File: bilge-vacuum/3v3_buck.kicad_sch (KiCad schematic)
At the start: 24 parts, among them Q1 PSMN014-80YL, Q2 PSMN014-80YL, U4 LTC3851

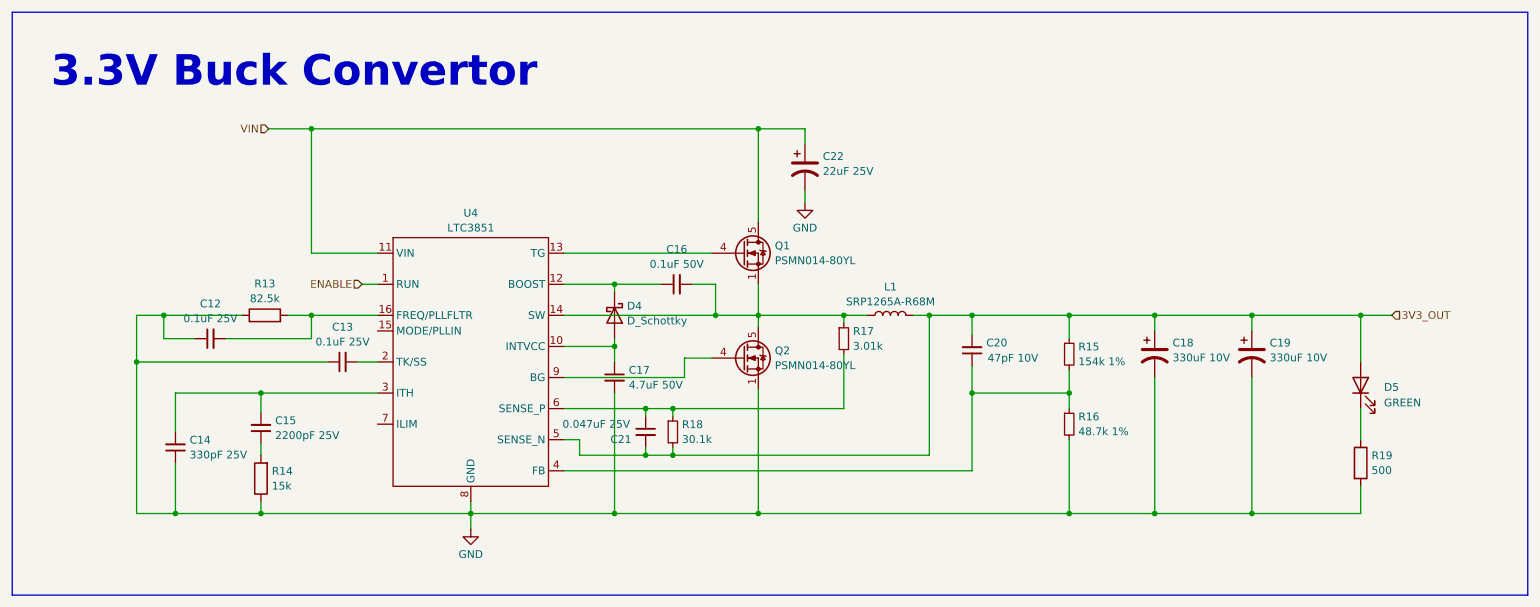
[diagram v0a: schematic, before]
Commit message: Assign the bulk of parts, some passives still need custom footprints.
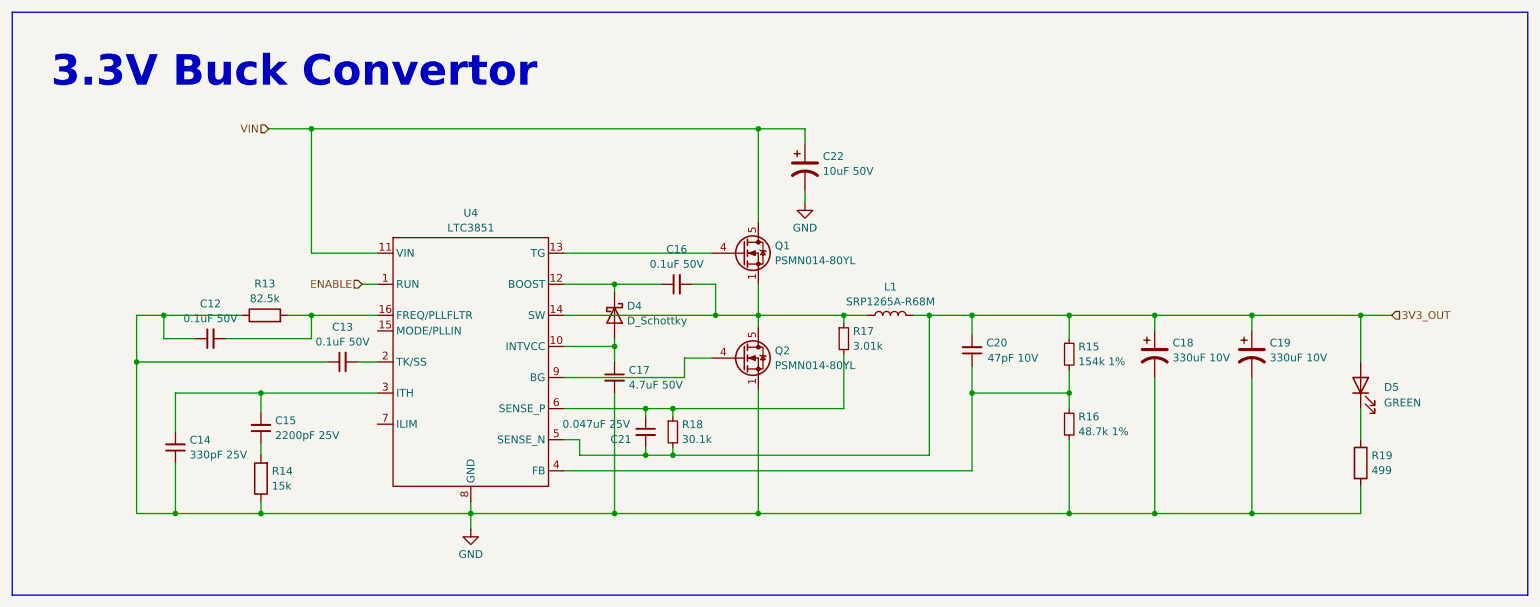
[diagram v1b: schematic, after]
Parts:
- C12, C13: value 0.1uF 25V -> 0.1uF 50V; footprint (none) -> Capacitor_SMD:C_0805_2012Metric
- C14, C15, C16, C17, C20, C21: footprint (none) -> Capacitor_SMD:C_0805_2012Metric
- C22: value 22uF 25V -> 10uF 50V; footprint (none) -> Capacitor_SMD:C_1206_3216Metric
- D4: footprint (none) -> Custom Parts:SMA
- D5: footprint (none) -> LED_SMD:LED_0805_2012Metric
- R13, R14, R15, R16, R17, R18: footprint (none) -> Resistor_SMD:R_0805_2012Metric
- R19: value 500 -> 499; footprint (none) -> Resistor_SMD:R_0805_2012Metric
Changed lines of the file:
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@@
       (effects (font (size 1.27 1.27)) (justify right))
     )
-    (property "Footprint" "" (at 239.395 80.01 0)
+    (property "Footprint" "LED_SMD:LED_0805_2012Metric" (at 239.395 80.01 0)
       (effects (font (size 1.27 1.27)) hide)
     )
@@
       (effects (font (size 1.27 1.27)) (justify left))
     )
-    (property "Footprint" "" (at 117.475 78.74 0)
+    (property "Footprint" "Capacitor_SMD:C_0805_2012Metric" (at 117.475 78.74 0)
       (effects (font (size 1.27 1.27)) hide)
     )
@@
       (effects (font (size 1.27 1.27)) (justify left))
     )
-    (property "Footprint" "" (at 127 87.63 0)
+    (property "Footprint" "Resistor_SMD:R_0805_2012Metric" (at 127 87.63 0)
       (effects (font (size 1.27 1.27)) hide)
     )
@@
       (effects (font (size 1.27 1.27)) (justify right))
     )
-    (property "Footprint" "" (at 61.468 95.25 90)
+    (property "Footprint" "Resistor_SMD:R_0805_2012Metric" (at 61.468 95.25 90)
       (effects (font (size 1.27 1.27)) hide)
     )
@@
       (effects (font (size 1.27 1.27)) (justify left))
     )
-    (property "Footprint" "" (at 117.475 68.58 0)
+    (property "Footprint" "Custom Parts:SMA" (at 117.475 68.58 0)
       (effects (font (size 1.27 1.27)) hide)
     )
@@
       (effects (font (size 1.27 1.27)) (justify right))
     )
-    (property "Footprint" "" (at 175.895 74.295 0)
+    (property "Footprint" "Capacitor_SMD:C_0805_2012Metric" (at 175.895 74.295 0)
       (effects (font (size 1.27 1.27)) hide)
     )
@@
       (effects (font (size 1.27 1.27)))
     )
-    (property "Value" "0.1uF 25V" (at 51.4413 69.1078 90)
-      (effects (font (size 1.27 1.27)))
-    )
-    (property "Footprint" "" (at 51.435 72.39 0)
+    (property "Value" "0.1uF 50V" (at 51.4413 69.1078 90)
+      (effects (font (size 1.27 1.27)))
+    )
+    (property "Footprint" "Capacitor_SMD:C_0805_2012Metric" (at 51.435 72.39 0)
       (effects (font (size 1.27 1.27)) hide)
     )
@@
       (effects (font (size 1.27 1.27)) (justify right))
     )
-    (property "Footprint" "" (at 122.555 87.63 0)
+    (property "Footprint" "Capacitor_SMD:C_0805_2012Metric" (at 122.555 87.63 0)
       (effects (font (size 1.27 1.27)) hide)
     )
@@
       (effects (font (size 1.27 1.27)) (justify left))
     )
-    (property "Footprint" "" (at 154.94 72.39 0)
+    (property "Footprint" "Resistor_SMD:R_0805_2012Metric" (at 154.94 72.39 0)
       (effects (font (size 1.27 1.27)) hide)
     )
@@
       (effects (font (size 1.27 1.27)) (justify right))
     )
-    (property "Footprint" "" (at 59.69 86.995 0)
+    (property "Footprint" "Capacitor_SMD:C_0805_2012Metric" (at 59.69 86.995 0)
       (effects (font (size 1.27 1.27)) hide)
     )
@@
       (effects (font (size 1.27 1.27)))
     )
-    (property "Value" "0.1uF 25V" (at 73.0313 72.9178 90)
-      (effects (font (size 1.27 1.27)))
-    )
-    (property "Footprint" "" (at 73.025 76.2 0)
+    (property "Value" "0.1uF 50V" (at 73.0313 72.9178 90)
+      (effects (font (size 1.27 1.27)))
+    )
+    (property "Footprint" "Capacitor_SMD:C_0805_2012Metric" (at 73.025 76.2 0)
       (effects (font (size 1.27 1.27)) hide)
     )
@@
       (effects (font (size 1.27 1.27)) (justify left))
     )
-    (property "Footprint" "" (at 191.77 74.93 0)
+    (property "Footprint" "Resistor_SMD:R_0805_2012Metric" (at 191.77 74.93 0)
       (effects (font (size 1.27 1.27)) hide)
     )
@@
       (effects (font (size 1.27 1.27)))
     )
-    (property "Footprint" "" (at 60.325 70.358 90)
+    (property "Footprint" "Resistor_SMD:R_0805_2012Metric" (at 60.325 70.358 90)
       (effects (font (size 1.27 1.27)) hide)
     )
@@
       (effects (font (size 1.27 1.27)) (justify left))
     )
-    (property "Value" "22uF 25V" (at 151.511 45.0271 0)
-      (effects (font (size 1.27 1.27)) (justify left))
-    )
-    (property "Footprint" "" (at 148.59 44.45 0)
+    (property "Value" "10uF 50V" (at 151.511 45.0271 0)
+      (effects (font (size 1.27 1.27)) (justify left))
+    )
+    (property "Footprint" "Capacitor_SMD:C_1206_3216Metric" (at 148.59 44.45 0)
       (effects (font (size 1.27 1.27)) hide)
     )
@@
       (effects (font (size 1.27 1.27)))
     )
-    (property "Footprint" "" (at 127.635 63.5 0)
+    (property "Footprint" "Capacitor_SMD:C_0805_2012Metric" (at 127.635 63.5 0)
       (effects (font (size 1.27 1.27)) hide)
     )
@@
       (effects (font (size 1.27 1.27)) (justify right))
     )
-    (property "Footprint" "" (at 45.72 90.17 0)
+    (property "Footprint" "Capacitor_SMD:C_0805_2012Metric" (at 45.72 90.17 0)
       (effects (font (size 1.27 1.27)) hide)
     )
@@
       (effects (font (size 1.27 1.27)) (justify left))
     )
-    (property "Value" "500" (at 241.173 93.9221 0)
-      (effects (font (size 1.27 1.27)) (justify left))
-    )
-    (property "Footprint" "" (at 237.617 92.71 90)
+    (property "Value" "499" (at 241.173 93.9221 0)
+      (effects (font (size 1.27 1.27)) (justify left))
+    )
+    (property "Footprint" "Resistor_SMD:R_0805_2012Metric" (at 237.617 92.71 90)
       (effects (font (size 1.27 1.27)) hide)
     )
@@
       (effects (font (size 1.27 1.27)) (justify left))
     )
-    (property "Footprint" "" (at 191.77 86.36 0)
-      (effects (font (size 1.27 1.27)) hide)
-    )
+    (property "Footprint" "Resistor_SMD:R_0805_2012Metric" (at 191.77 86.36 0)
+      (effects (font (size 1.27 1.27)) hide)
+    )

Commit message: Vac progress
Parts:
- C18, C19: value 330uF 10V -> EEE-FK1A331AV; footprint (none) -> Custom Parts:Panasonic - F - Vibe
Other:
- moved on the sheet: C19
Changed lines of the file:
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@@
     (stroke (width 0) (type default))
   )
-  (wire (pts (xy 221.615 78.74) (xy 221.615 100.965))
+  (wire (pts (xy 221.615 90.17) (xy 221.615 100.965))
     (stroke (width 0) (type default))
   )
@@
     (stroke (width 0) (type default))
   )
-  (wire (pts (xy 221.615 68.58) (xy 221.615 71.12))
+  (wire (pts (xy 221.615 68.58) (xy 221.615 82.55))
     (stroke (width 0) (type default))
   )
@@
       (effects (font (size 1.27 1.27)) (justify left))
     )
-    (property "Value" "330uF 10V" (at 208.661 75.5071 0)
-      (effects (font (size 1.27 1.27)) (justify left))
-    )
-    (property "Footprint" "" (at 205.74 74.93 0)
+    (property "Value" "EEE-FK1A331AV" (at 208.661 75.5071 0)
+      (effects (font (size 1.27 1.27)) (justify left))
+    )
+    (property "Footprint" "Custom Parts:Panasonic - F - Vibe" (at 205.74 74.93 0)
       (effects (font (size 1.27 1.27)) hide)
     )
@@
     )
   )
-  (symbol (lib_id "Device:C_Polarized_US") (at 221.615 74.93 0) (unit 1)
-    (in_bom yes) (on_board yes) (dnp no) (fields_autoplaced)
-    (property "Reference" "C19" (at 224.536 73.0829 0)
-      (effects (font (size 1.27 1.27)) (justify left))
-    )
-    (property "Value" "330uF 10V" (at 224.536 75.5071 0)
-      (effects (font (size 1.27 1.27)) (justify left))
-    )
-    (property "Footprint" "" (at 221.615 74.93 0)
-      (effects (font (size 1.27 1.27)) hide)
-    )
-    (property "Datasheet" "~" (at 221.615 74.93 0)
-      (effects (font (size 1.27 1.27)) hide)
-    )
+  (symbol (lib_id "Device:C_Polarized_US") (at 221.615 86.36 0) (unit 1)
+    (in_bom yes) (on_board yes) (dnp no) (fields_autoplaced)
+    (property "Reference" "C19" (at 224.536 84.5129 0)
+      (effects (font (size 1.27 1.27)) (justify left))
+    )
+    (property "Value" "EEE-FK1A331AV" (at 224.536 86.9371 0)
+      (effects (font (size 1.27 1.27)) (justify left))
+    )
+    (property "Footprint" "Custom Parts:Panasonic - F - Vibe" (at 221.615 86.36 0)
+      (effects (font (size 1.27 1.27)) hide)
+    )
+    (property "Datasheet" "~" (at 221.615 86.36 0)
+      (effects (font (size 1.27 1.27)) hide)
+    )

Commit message: bilge vac 1v0
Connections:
- net BUCK_BG: now reaches Q2.4 (G), U4.9 (BG)
- net BUCK_TG: now reaches Q1.4 (G), U4.13 (TG)
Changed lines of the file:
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@@
     (effects (font (size 5 5) bold) (justify left bottom))
+  )
+  (label "BUCK_TG" (at 111.76 58.42 0) (fields_autoplaced)
+    (effects (font (size 1.27 1.27)) (justify left bottom))
+  )
+  (label "BUCK_BG" (at 111.76 78.74 0) (fields_autoplaced)
+    (effects (font (size 1.27 1.27)) (justify left bottom))
   )
   (hierarchical_label "3V3_OUT" (shape input) (at 244.475 68.58 0) (fields_autoplaced)

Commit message: Fixes
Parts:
- added C22 (x2): 10uF 50V, Capacitor_SMD:C_1206_3216Metric, symbol Device:C_Small
- C22: symbol Device:C_Polarized_US -> Device:C_Small
- D4: value D_Schottky -> B260AQ-13-F
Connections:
- net GND: now also C22.2, C22.2
- net VIN: now also C22.1, C22.1
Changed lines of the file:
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@@
   (junction (at 205.74 100.965) (diameter 0) (color 0 0 0 0)
   )
+  (junction (at 163.83 38.1) (diameter 0) (color 0 0 0 0)
+  )
   (junction (at 117.475 73.66) (diameter 0) (color 0 0 0 0)
   )
   (junction (at 59.69 81.28) (diameter 0) (color 0 0 0 0)
   )
+  (junction (at 148.59 50.8) (diameter 0) (color 0 0 0 0)
+  )
   (junction (at 175.895 81.28) (diameter 0) (color 0 0 0 0)
   )
+  (junction (at 148.59 38.1) (diameter 0) (color 0 0 0 0)
+  )
   (junction (at 122.555 83.82) (diameter 0) (color 0 0 0 0)
   )
@@
   (junction (at 140.97 100.965) (diameter 0) (color 0 0 0 0)
   )
+  (junction (at 163.83 50.8) (diameter 0) (color 0 0 0 0)
+  )
   (junction (at 191.77 81.28) (diameter 0) (color 0 0 0 0)
   )
@@
     (stroke (width 0) (type default))
   )
+  (wire (pts (xy 163.83 47.625) (xy 163.83 50.8))
+    (stroke (width 0) (type default))
+  )
   (wire (pts (xy 67.945 58.42) (xy 67.945 38.1))
     (stroke (width 0) (type default))
@@
     (stroke (width 0) (type default))
   )
-  (wire (pts (xy 148.59 40.64) (xy 148.59 38.1))
-    (stroke (width 0) (type default))
-  )
   (wire (pts (xy 140.97 38.1) (xy 140.97 53.34))
     (stroke (width 0) (type default))
@@
     (stroke (width 0) (type default))
   )
+  (wire (pts (xy 163.83 50.8) (xy 179.07 50.8))
+    (stroke (width 0) (type default))
+  )
   (wire (pts (xy 239.395 68.58) (xy 239.395 76.2))
     (stroke (width 0) (type default))
@@
     (stroke (width 0) (type default))
   )
+  (wire (pts (xy 148.59 50.8) (xy 148.59 52.705))
+    (stroke (width 0) (type default))
+  )
   (wire (pts (xy 39.37 76.2) (xy 39.37 68.58))
     (stroke (width 0) (type default))
@@
     (stroke (width 0) (type default))
   )
+  (wire (pts (xy 148.59 38.1) (xy 148.59 42.545))
+    (stroke (width 0) (type default))
+  )
   (wire (pts (xy 59.69 81.28) (xy 45.72 81.28))
     (stroke (width 0) (type default))
   )
+  (wire (pts (xy 148.59 50.8) (xy 163.83 50.8))
+    (stroke (width 0) (type default))
+  )
   (wire (pts (xy 78.74 58.42) (xy 67.945 58.42))
     (stroke (width 0) (type default))
@@
     (stroke (width 0) (type default))
   )
+  (wire (pts (xy 163.83 38.1) (xy 179.07 38.1))
+    (stroke (width 0) (type default))
+  )
+  (wire (pts (xy 148.59 38.1) (xy 163.83 38.1))
+    (stroke (width 0) (type default))
+  )
   (wire (pts (xy 59.69 100.965) (xy 59.69 99.06))
     (stroke (width 0) (type default))
@@
     (stroke (width 0) (type default))
   )
+  (wire (pts (xy 179.07 47.625) (xy 179.07 50.8))
+    (stroke (width 0) (type default))
+  )
   (wire (pts (xy 127 83.82) (xy 122.555 83.82))
     (stroke (width 0) (type default))
@@
     (stroke (width 0) (type default))
   )
+  (wire (pts (xy 179.07 38.1) (xy 179.07 42.545))
+    (stroke (width 0) (type default))
+  )
   (wire (pts (xy 205.74 68.58) (xy 221.615 68.58))
     (stroke (width 0) (type default))
@@
     (stroke (width 0) (type default))
   )
+  (wire (pts (xy 163.83 38.1) (xy 163.83 42.545))
+    (stroke (width 0) (type default))
+  )
   (wire (pts (xy 43.815 68.58) (xy 43.815 72.39))
     (stroke (width 0) (type default))
@@
     (stroke (width 0) (type default))
   )
-  (wire (pts (xy 148.59 48.26) (xy 148.59 50.165))
-    (stroke (width 0) (type default))
-  )
   (wire (pts (xy 221.615 68.58) (xy 239.395 68.58))
     (stroke (width 0) (type default))
@@
   )
   (wire (pts (xy 205.74 68.58) (xy 205.74 71.12))
+    (stroke (width 0) (type default))
+  )
+  (wire (pts (xy 148.59 47.625) (xy 148.59 50.8))
     (stroke (width 0) (type default))
   )
@@
       (effects (font (size 1.27 1.27)) (justify left))
     )
-    (property "Value" "D_Schottky" (at 119.507 69.4746 90)
+    (property "Value" "B260AQ-13-F" (at 119.507 69.4746 90)
       (effects (font (size 1.27 1.27)) (justify left))
     )
@@
     )
   )
-  (symbol (lib_id "power:GND") (at 148.59 50.165 0) (unit 1)
-    (in_bom yes) (on_board yes) (dnp no) (fields_autoplaced)
-    (property "Reference" "#PWR018" (at 148.59 56.515 0)
-      (effects (font (size 1.27 1.27)) hide)
-    )
-    (property "Value" "GND" (at 148.59 54.2981 0)
+  (symbol (lib_id "power:GND") (at 148.59 52.705 0) (unit 1)
+    (in_bom yes) (on_board yes) (dnp no) (fields_autoplaced)
+    (property "Reference" "#PWR018" (at 148.59 59.055 0)
+      (effects (font (size 1.27 1.27)) hide)
+    )
+    (property "Value" "GND" (at 148.59 56.8381 0)
       (effects (font (size 1.27 1.27)))
     )
-    (property "Footprint" "" (at 148.59 50.165 0)
-      (effects (font (size 1.27 1.27)) hide)
-    )
-    (property "Datasheet" "" (at 148.59 50.165 0)
+    (property "Footprint" "" (at 148.59 52.705 0)
+      (effects (font (size 1.27 1.27)) hide)
+    )
+    (property "Datasheet" "" (at 148.59 52.705 0)
       (effects (font (size 1.27 1.27)) hide)
     )
@@
     )
   )
+  (symbol (lib_id "Device:C_Small") (at 179.07 45.085 0) (unit 1)
+    (in_bom yes) (on_board yes) (dnp no) (fields_autoplaced)
+    (property "Reference" "C22" (at 181.991 43.2379 0)
+      (effects (font (size 1.27 1.27)) (justify left))
+    )
+    (property "Value" "10uF 50V" (at 181.991 45.6621 0)
+      (effects (font (size 1.27 1.27)) (justify left))
+    )
+    (property "Footprint" "Capacitor_SMD:C_1206_3216Metric" (at 179.07 45.085 0)
+      (effects (font (size 1.27 1.27)) hide)
+    )
+    (property "Datasheet" "~" (at 179.07 45.085 0)
+      (effects (font (size 1.27 1.27)) hide)
+    )
+    (pin "1")
+    (pin "2")
+    (instances
+      (project "bilge-vacuum"
+        (path "/08405ba3-6912-4dc1-869a-b11176a5bc8a"
+          (reference "C22") (unit 1)
+        )
+        (path "/08405ba3-6912-4dc1-869a-b11176a5bc8a/8a95e837-e0e7-4b78-93e7-7ab95e7c82dc/f4009a8b-181d-4005-8c08-1454b9ebf288"
+          (reference "C55") (unit 1)
+        )
+      )
+    )
+  )
   (symbol (lib_id "Device:R") (at 60.325 68.58 90) (unit 1)
     (in_bom yes) (on_board yes) (dnp no) (fields_autoplaced)
@@
     )
   )
-  (symbol (lib_id "Device:C_Polarized_US") (at 148.59 44.45 0) (unit 1)
-    (in_bom yes) (on_board yes) (dnp no) (fields_autoplaced)
-    (property "Reference" "C22" (at 151.511 42.6029 0)
-      (effects (font (size 1.27 1.27)) (justify left))
-    )
-    (property "Value" "10uF 50V" (at 151.511 45.0271 0)
-      (effects (font (size 1.27 1.27)) (justify left))
-    )
-    (property "Footprint" "Capacitor_SMD:C_1206_3216Metric" (at 148.59 44.45 0)
-      (effects (font (size 1.27 1.27)) hide)
-    )
-    (property "Datasheet" "~" (at 148.59 44.45 0)
+  (symbol (lib_id "Device:C_Small") (at 148.59 45.085 0) (unit 1)
+    (in_bom yes) (on_board yes) (dnp no) (fields_autoplaced)
+    (property "Reference" "C22" (at 151.511 43.2379 0)
+      (effects (font (size 1.27 1.27)) (justify left))
+    )
+    (property "Value" "10uF 50V" (at 151.511 45.6621 0)
+      (effects (font (size 1.27 1.27)) (justify left))
+    )
+    (property "Footprint" "Capacitor_SMD:C_1206_3216Metric" (at 148.59 45.085 0)
+      (effects (font (size 1.27 1.27)) hide)
+    )
+    (property "Datasheet" "~" (at 148.59 45.085 0)
       (effects (font (size 1.27 1.27)) hide)
     )
@@
         )
       )
+    )
+  )
+  (symbol (lib_id "Device:C_Small") (at 163.83 45.085 0) (unit 1)
+    (in_bom yes) (on_board yes) (dnp no) (fields_autoplaced)
+    (property "Reference" "C22" (at 166.751 43.2379 0)
+      (effects (font (size 1.27 1.27)) (justify left))
+    )
+    (property "Value" "10uF 50V" (at 166.751 45.6621 0)
+      (effects (font (size 1.27 1.27)) (justify left))
+    )
+    (property "Footprint" "Capacitor_SMD:C_1206_3216Metric" (at 163.83 45.085 0)
+      (effects (font (size 1.27 1.27)) hide)
+    )
+    (property "Datasheet" "~" (at 163.83 45.085 0)
+      (effects (font (size 1.27 1.27)) hide)
+    )
+    (pin "1")
+    (pin "2")
+    (instances
+      (project "bilge-vacuum"
+        (path "/08405ba3-6912-4dc1-869a-b11176a5bc8a"
+          (reference "C22") (unit 1)
+        )
+        (path "/08405ba3-6912-4dc1-869a-b11176a5bc8a/8a95e837-e0e7-4b78-93e7-7ab95e7c82dc/f4009a8b-181d-4005-8c08-1454b9ebf288"
+          (reference "C54") (unit 1)
+        )
+      )
